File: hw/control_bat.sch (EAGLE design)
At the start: 5 parts, among them X1 DF13-4P-1.25V(50)

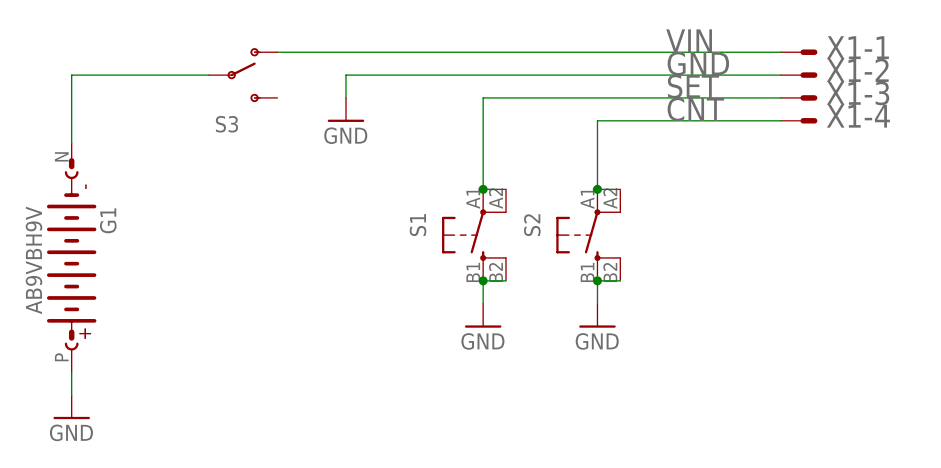
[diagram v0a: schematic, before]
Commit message: Fix battery orientation in control board. Panelize for manufacturing.
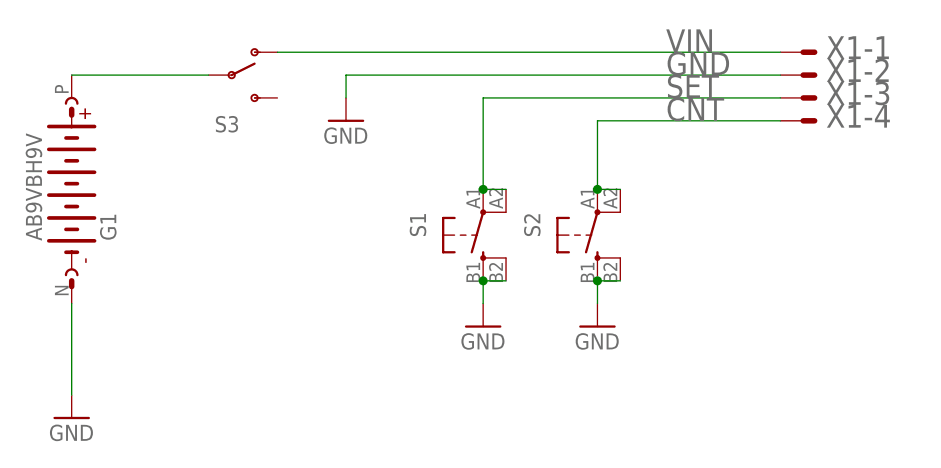
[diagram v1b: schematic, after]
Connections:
- net GND: now also G1.-; no longer G1.+
- net N$4: now also G1.+; no longer G1.-
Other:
- moved on the sheet: G1
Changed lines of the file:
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@@
 <instance part="GND4" gate="1" x="43.18" y="48.26"/>
 <instance part="S3" gate="1" x="30.48" y="53.34"/>
-<instance part="G1" gate="G$1" x="12.7" y="33.02" rot="R270"/>
+<instance part="G1" gate="G$1" x="12.7" y="40.64" rot="MR90"/>
 </instances>
 <busses>
@@
 <pinref part="GND4" gate="1" pin="GND"/>
 <wire x1="43.18" y1="53.34" x2="43.18" y2="50.8" width="0.1524" layer="91"/>
-</segment>
-<segment>
-<pinref part="GND1" gate="1" pin="GND"/>
-<wire x1="12.7" y1="17.78" x2="12.7" y2="20.32" width="0.1524" layer="91"/>
-<pinref part="G1" gate="G$1" pin="+"/>
 </segment>
 <segment>
@@
 <wire x1="71.12" y1="27.94" x2="71.12" y2="30.48" width="0.1524" layer="91"/>
 <junction x="71.12" y="30.48"/>
+</segment>
+<segment>
+<pinref part="G1" gate="G$1" pin="-"/>
+<pinref part="GND1" gate="1" pin="GND"/>
+<wire x1="12.7" y1="27.94" x2="12.7" y2="17.78" width="0.1524" layer="91"/>
 </segment>
 </net>
@@
 <net name="N$4" class="0">
 <segment>
-<wire x1="12.7" y1="45.72" x2="12.7" y2="53.34" width="0.1524" layer="91"/>
 <pinref part="S3" gate="1" pin="P"/>
 <wire x1="12.7" y1="53.34" x2="27.94" y2="53.34" width="0.1524" layer="91"/>
-<pinref part="G1" gate="G$1" pin="-"/>
+<pinref part="G1" gate="G$1" pin="+"/>
 </segment>
 </net>
